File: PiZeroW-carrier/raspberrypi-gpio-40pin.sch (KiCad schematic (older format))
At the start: 8 parts, among them J1 PI40HAT, J2 CONN_02X02

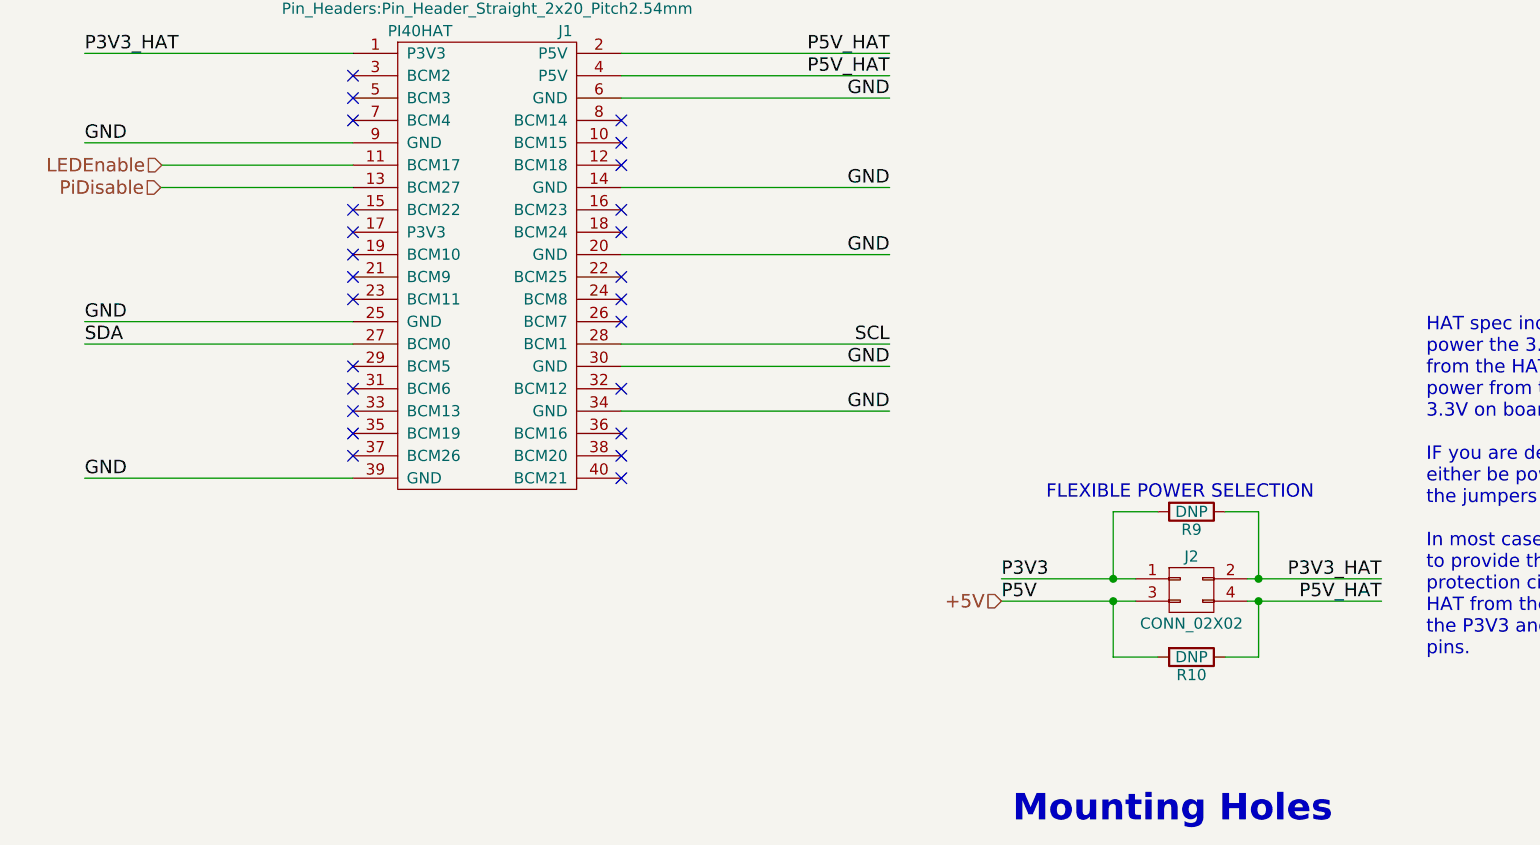
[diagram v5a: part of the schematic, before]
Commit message: Before Trace fix of LED AND PIDISABLE
Push before tracing fix of LEDEnable and PIDisable
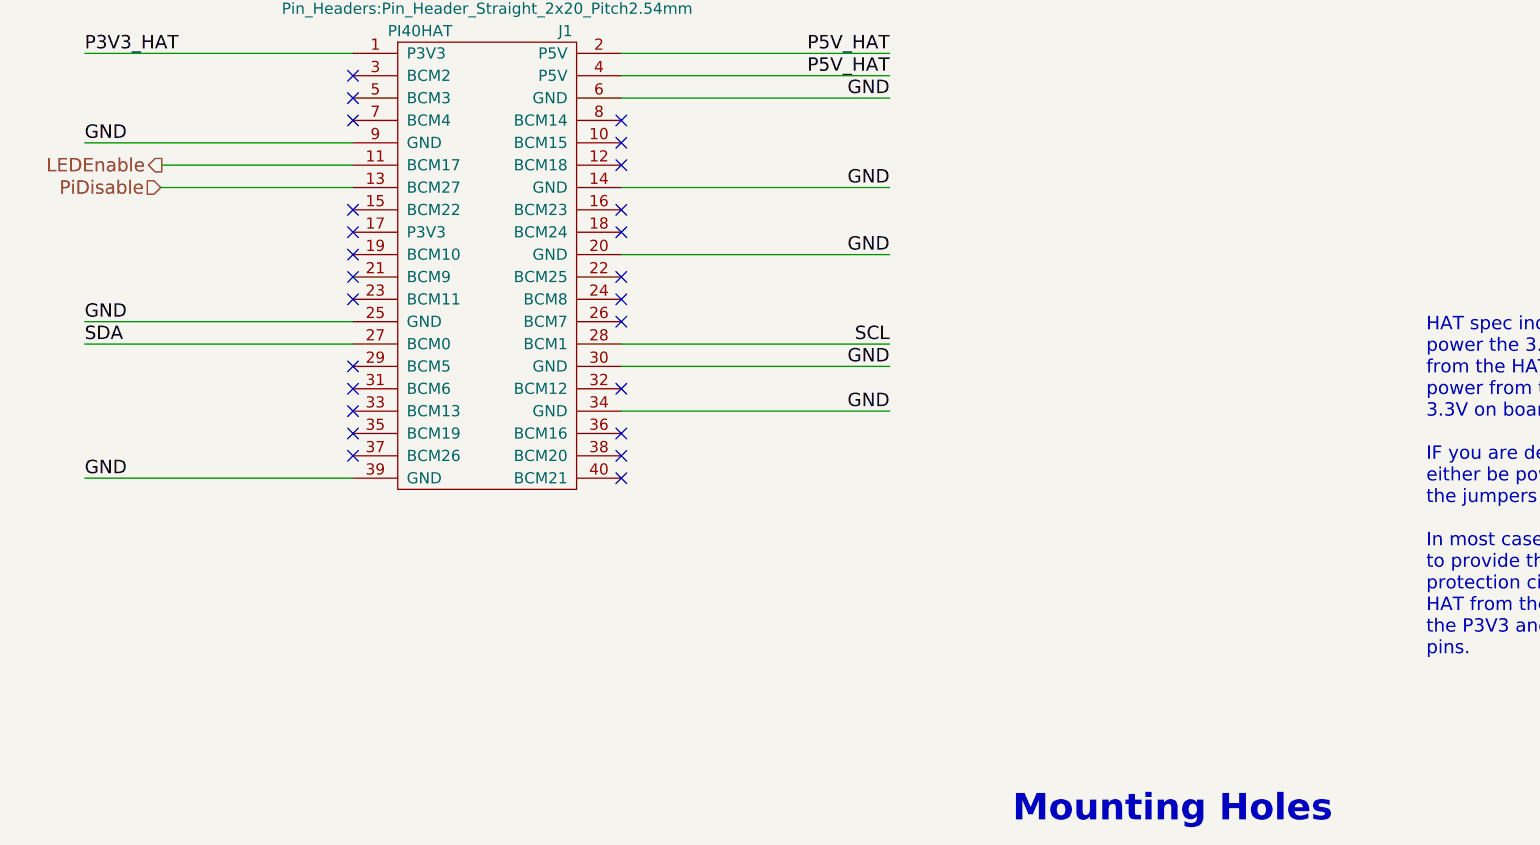
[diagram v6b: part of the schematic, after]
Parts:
- removed J2: CONN_02X02, Pin_Headers:Pin_Header_Straight_2x02_Pitch2.54mm, symbol CONN_02X02
- removed R10, R9: DNP, Resistors_SMD:R_0805_HandSoldering, symbol R
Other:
- note removed: "FLEXIBLE POWER SELECTION"
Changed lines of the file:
@@
 Comment4 ""
 $EndDescr
-$Comp
-L CONN_02X02 J2
-U 1 1 5A256562
-P 6100 4650
-F 0 "J2" H 6100 4800 50  0000 C CNN
-F 1 "CONN_02X02" H 6100 4500 50  0000 C CNN
-F 2 "Pin_Headers:Pin_Header_Straight_2x02_Pitch2.54mm" H 6100 3450 50  0001 C CNN
-F 3 "" H 6100 3450 50  0000 C CNN
-	1    6100 4650
-	1    0    0    -1
-$EndComp
-Text Label 5250 4600 0    60   ~ 0
-P3V3
-Text Label 5250 4700 0    60   ~ 0
-P5V
-Wire Wire Line
-	5250 4600 5850 4600
-Wire Wire Line
-	5250 4700 5850 4700
-Text Label 6950 4600 2    60   ~ 0
-P3V3_HAT
-Text Label 6950 4700 2    60   ~ 0
-P5V_HAT
-Wire Wire Line
-	6350 4600 6950 4600
-Wire Wire Line
-	6350 4700 6950 4700
-Text Notes 5450 4250 0    60   ~ 0
-FLEXIBLE POWER SELECTION
-$Comp
-L R R9
-U 1 1 5A256571
-P 6100 4300
-F 0 "R9" V 6180 4300 50  0000 C CNN
-F 1 "DNP" V 6100 4300 50  0000 C CNN
-F 2 "Resistors_SMD:R_0805_HandSoldering" V 6030 4300 50  0001 C CNN
-F 3 "" H 6100 4300 50  0001 C CNN
-F 4 "Yageo" H -9450 -10050 50  0001 C CNN "MFR"
-F 5 "RC0402JR-0722RL" H -9450 -10050 50  0001 C CNN "MPN"
-F 6 "Digikey" H -9450 -10050 50  0001 C CNN "SPR"
-F 7 "311-22JRCT-ND" H -9450 -10050 50  0001 C CNN "SPN"
-F 8 "" H -9450 -10050 50  0001 C CNN "SPURL"
-	1    6100 4300
-	0    1    1    0
-$EndComp
-$Comp
-L R R10
-U 1 1 5A256572
-P 6100 4950
-F 0 "R10" V 6180 4950 50  0000 C CNN
-F 1 "DNP" V 6100 4950 50  0000 C CNN
-F 2 "Resistors_SMD:R_0805_HandSoldering" V 6030 4950 50  0001 C CNN
-F 3 "" H 6100 4950 50  0001 C CNN
-F 4 "Yageo" H -9450 -9400 50  0001 C CNN "MFR"
-F 5 "RC0402JR-0722RL" H -9450 -9400 50  0001 C CNN "MPN"
-F 6 "Digikey" H -9450 -9400 50  0001 C CNN "SPR"
-F 7 "311-22JRCT-ND" H -9450 -9400 50  0001 C CNN "SPN"
-F 8 "" H -9450 -9400 50  0001 C CNN "SPURL"
-	1    6100 4950
-	0    1    1    0
-$EndComp
-Wire Wire Line
-	5750 4700 5750 4950
-Wire Wire Line
-	5750 4950 5950 4950
-Connection ~ 5750 4700
-Wire Wire Line
-	6250 4950 6400 4950
-Wire Wire Line
-	6400 4950 6400 4700
-Connection ~ 6400 4700
-Wire Wire Line
-	6400 4600 6400 4300
-Wire Wire Line
-	6400 4300 6250 4300
-Connection ~ 6400 4600
-Wire Wire Line
-	5950 4300 5750 4300
-Wire Wire Line
-	5750 4300 5750 4600
-Connection ~ 5750 4600
 Text Notes 5300 5700 0    118  ~ 24
 Mounting Holes
@@
 Text Notes 850  1250 0    100  ~ 0
 This is based on the official Raspberry Pi spec to be able to call an extension board a HAT.\nhttps://github.com/raspberrypi/hats/blob/master/designguide.md
-Text HLabel 5250 4700 0    60   Input ~ 0
-+5V
-Text HLabel 1495 2750 0    60   Input ~ 0
-LEDEnable
 Wire Wire Line
 	1495 2750 2350 2750
@@
 	1    0    0    -1
 $EndComp
+Text HLabel 1495 2750 0    60   Output ~ 0
+LEDEnable
 $EndSCHEMATC

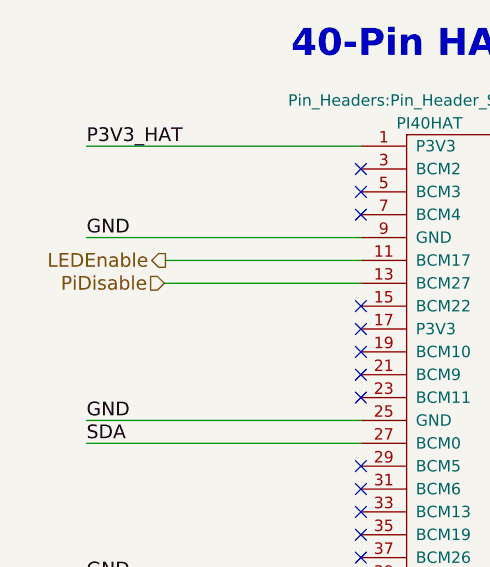
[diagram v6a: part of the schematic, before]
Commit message: PCb Now with PIDisable and 6V Connection.
Featuring a PCB With proper PIDisable and 6V Connections
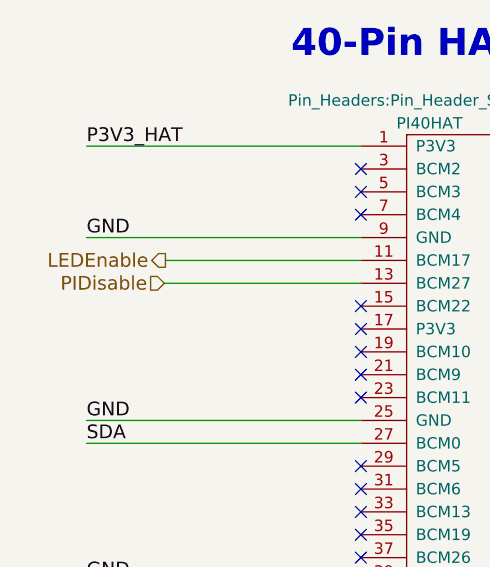
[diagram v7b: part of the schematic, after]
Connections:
- net PiDisable renamed PIDisable
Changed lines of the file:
@@
 Text Label 4750 2250 2    60   ~ 0
 P5V_HAT
-Text HLabel 1490 2850 0    60   Input ~ 0
-PiDisable
 Wire Wire Line
 	1490 2850 2350 2850
@@
 Text HLabel 1495 2750 0    60   Output ~ 0
 LEDEnable
+Text HLabel 1490 2850 0    60   Input ~ 0
+PIDisable
 $EndSCHEMATC
